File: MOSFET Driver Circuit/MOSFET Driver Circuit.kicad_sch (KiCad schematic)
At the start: 5 parts, among them Q1 NDT3055L

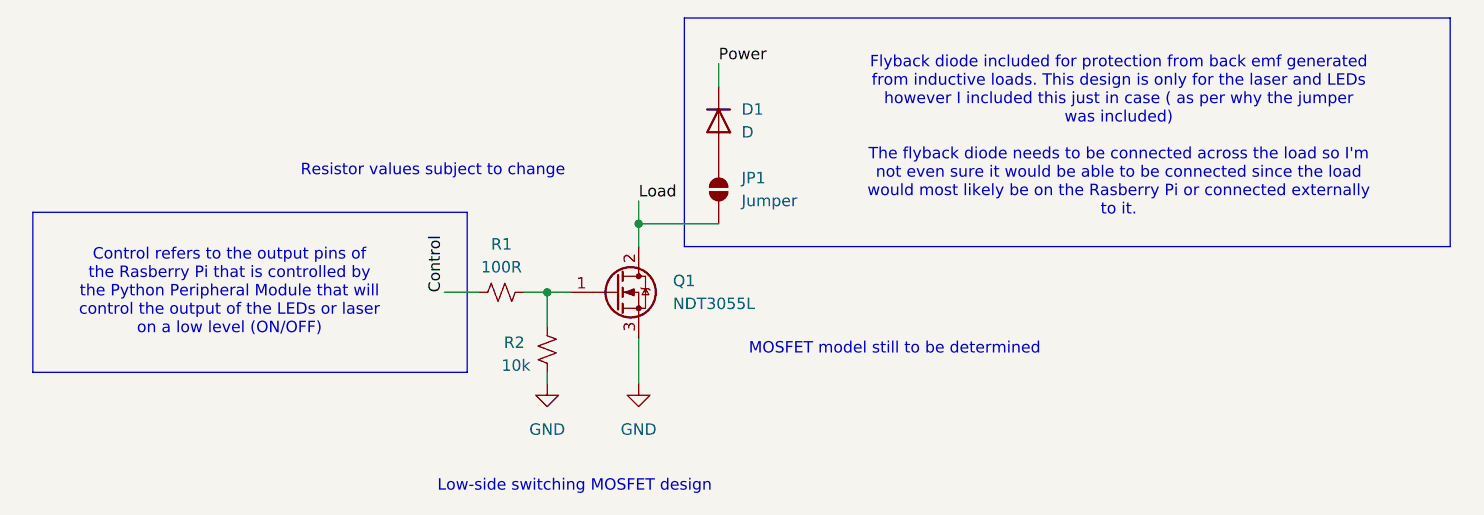
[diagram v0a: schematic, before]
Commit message: Updates
Updated the MOSFET driver circuits and created the toggle and PWM control functions for the lasers in the aqua_io.py python module

Added a relationship table for the pins on the RPi5
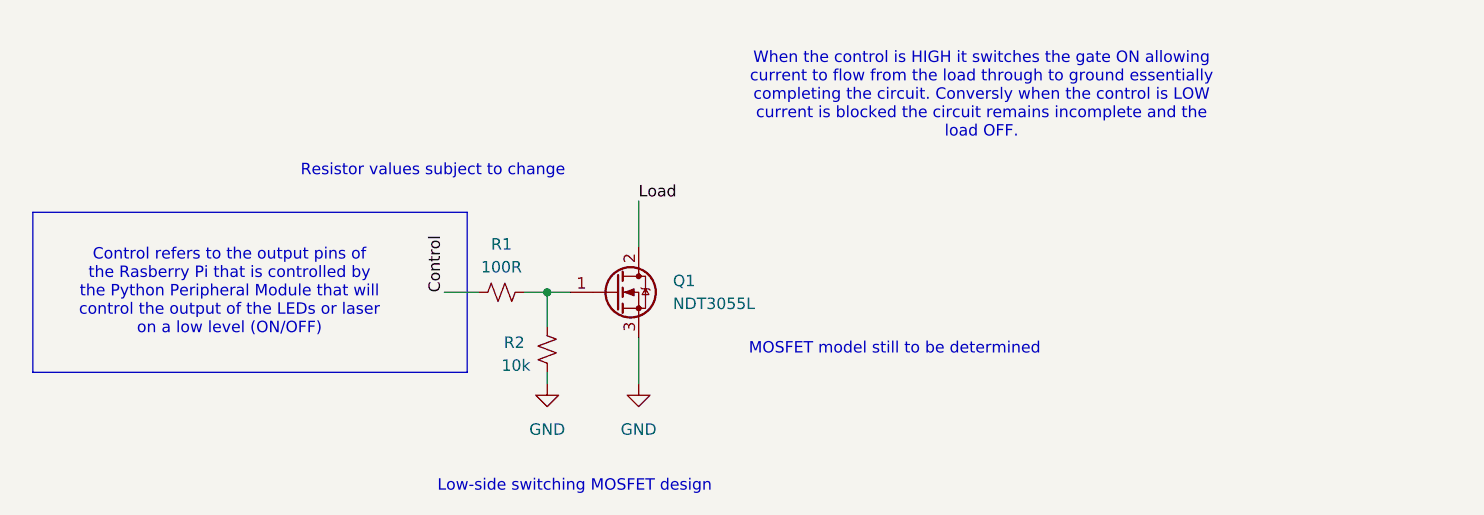
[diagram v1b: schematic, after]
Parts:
- removed D1: D, symbol Device:D
- removed JP1: Jumper, symbol Jumper:SolderJumper_2_Open
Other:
- note added: "When the control is HIGH it switches the gate ON allowing current to flow from the load through to ground essentially completing the circuit. Conversly when the control is LOW current is blocked the circuit remains incomplete and the load OFF."
- note removed: "Flyback diode included for protection from back emf generated from inductive loads. This design is only for the laser and LEDs however I included this just in case ( as per why the jumper was included) The flyback diode needs to be connected across the load so I'm not even sure it would be able to be connected since the load would most likely be on the Rasberry Pi or connected externally to it."
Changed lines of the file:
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@@
-		)
-	)
-	(rectangle
-		(start 163.83 121.92)
-		(end 248.92 147.32)
-		(stroke
-			(width 0)
-			(type default)
-		)
-		(fill
-			(type none)
 		)
 	)
@@
 		)
 	)
-	(text "Flyback diode included for protection from back emf generated \nfrom inductive loads. This design is only for the laser and LEDs\nhowever I included this just in case ( as per why the jumper\nwas included)\n\nThe flyback diode needs to be connected across the load so I'm\nnot even sure it would be able to be connected since the load\nwould most likely be on the Rasberry Pi or connected externally \nto it."
-		(exclude_from_sim no)
-		(at 212.09 135.128 0)
+	(text "When the control is HIGH it switches the gate ON allowing\ncurrent to flow from the load through to ground essentially \ncompleting the circuit. Conversly when the control is LOW \ncurrent is blocked the circuit remains incomplete and the\nload OFF."
+		(exclude_from_sim no)
+		(at 196.85 130.556 0)
 		(effects
 			(font
@@
 		(color 0 0 0 0)
 	)
-	(junction
-		(at 158.75 144.78)
-		(diameter 0)
-		(color 0 0 0 0)
-	)
 	(wire
 		(pts
@@
 	(wire
 		(pts
-			(xy 158.75 144.78) (xy 158.75 147.32)
+			(xy 158.75 142.24) (xy 158.75 147.32)
 		)
 		(stroke
@@
 	(wire
 		(pts
-			(xy 158.75 144.78) (xy 167.64 144.78)
-		)
-		(stroke
-			(width 0)
-			(type default)
-		)
-	)
-	(wire
-		(pts
 			(xy 137.16 152.4) (xy 140.97 152.4)
 		)
@@
 	(wire
 		(pts
-			(xy 158.75 142.24) (xy 158.75 144.78)
-		)
-		(stroke
-			(width 0)
-			(type default)
-		)
-	)
-	(wire
-		(pts
 			(xy 148.59 161.29) (xy 148.59 162.56)
 		)
@@
 		)
 	)
-	(wire
-		(pts
-			(xy 167.64 127) (xy 167.64 129.54)
-		)
-		(stroke
-			(width 0)
-			(type default)
+	(label "Control"
+		(at 137.16 152.4 90)
+		(effects
+			(font
+				(size 1.27 1.27)
+			)
+			(justify left bottom)
 		)
 	)
 	(label "Load"
 		(at 158.75 142.24 0)
-		(effects
-			(font
-				(size 1.27 1.27)
-			)
-			(justify left bottom)
-		)
-	)
-	(label "Control"
-		(at 137.16 152.4 90)
-		(effects
-			(font
-				(size 1.27 1.27)
-			)
-			(justify left bottom)
-		)
-	)
-	(label "Power"
-		(at 167.64 127 0)
 		(effects
 			(font
@@
 	)
 	(symbol
-		(lib_id "Device:D")
-		(at 167.64 133.35 270)
-		(unit 1)
-		(exclude_from_sim no)
-		(in_bom yes)
-		(on_board yes)
-		(dnp no)
-		(fields_autoplaced yes)
-		(property "Reference" "D1"
-			(at 170.18 132.0799 90)
-			(effects
-				(font
-					(size 1.27 1.27)
-				)
-				(justify left)
-			)
-		)
-		(property "Value" "D"
-			(at 170.18 134.6199 90)
-			(effects
-				(font
-					(size 1.27 1.27)
-				)
-				(justify left)
-			)
-		)
-		(property "Footprint" ""
-			(at 167.64 133.35 0)
-			(effects
-				(font
-					(size 1.27 1.27)
-				)
-				(hide yes)
-			)
-		)
-		(property "Datasheet" "~"
-			(at 167.64 133.35 0)
-			(effects
-				(font
-					(size 1.27 1.27)
-				)
-				(hide yes)
-			)
-		)
-		(property "Description" "Diode"
-			(at 167.64 133.35 0)
-			(effects
-				(font
-					(size 1.27 1.27)
-				)
-				(hide yes)
-			)
-		)
-		(property "Sim.Device" "D"
-			(at 167.64 133.35 0)
-			(effects
-				(font
-					(size 1.27 1.27)
-				)
-				(hide yes)
-			)
-		)
-		(property "Sim.Pins" "1=K 2=A"
-			(at 167.64 133.35 0)
-			(effects
-				(font
-					(size 1.27 1.27)
-				)
-				(hide yes)
-			)
-		)
-		(pin "2"
-		)
-		(pin "1"
-		)
-		(instances
-			(project ""
-				(path "/435687ed-7edd-4a45-a329-a0e1ed3ec891"
-					(reference "D1")
-					(unit 1)
-				)
-			)
-		)
-	)
-	(symbol
 		(lib_id "Device:R_Small_US")
 		(at 143.51 152.4 90)
@@
 					(unit 1)
 				)
-			)
-		)
-	)
-	(symbol
-		(lib_id "Jumper:SolderJumper_2_Open")
-		(at 167.64 140.97 90)
-		(unit 1)
-		(exclude_from_sim no)
-		(in_bom no)
-		(on_board yes)
-		(dnp no)
-		(fields_autoplaced yes)
-		(property "Reference" "JP1"
-			(at 170.18 139.6999 90)
-			(effects
-				(font
-					(size 1.27 1.27)
-				)
-				(justify right)
-			)
-		)
-		(property "Value" "Jumper"
-			(at 170.18 142.2399 90)
-			(effects
-				(font
-					(size 1.27 1.27)
-				)
-				(justify right)
-			)
-		)
-		(property "Footprint" ""
-			(at 167.64 140.97 0)
-			(effects
-				(font
-					(size 1.27 1.27)
-				)
-				(hide yes)
-			)
-		)
-		(property "Datasheet" "~"
-			(at 167.64 140.97 0)
-			(effects
-				(font
-					(size 1.27 1.27)
-				)
-				(hide yes)
-			)
-		)
-		(property "Description" "Solder Jumper, 2-pole, open"
-			(at 167.64 140.97 0)
-			(effects
-				(font
-					(size 1.27 1.27)
-				)
-				(hide yes)
-			)
-		)
-		(pin "2"
-		)
-		(pin "1"
-		)
-		(instances
-			(project ""
-				(path "/435687ed-7edd-4a45-a329-a0e1ed3ec891"
-					(reference "JP1")
-					(unit 1)
-				)

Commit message: Updates
Completed MOSFET driver circuit design

Removed x,y,z limit switches from aqua_io.py

Assigned more GPIO pins
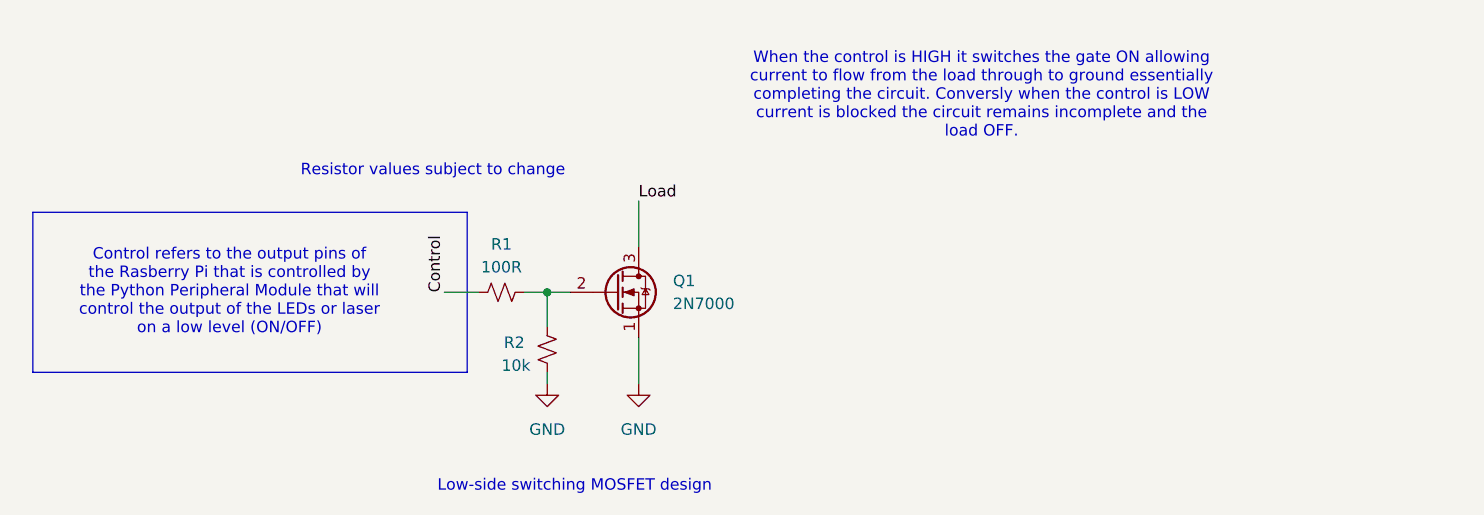
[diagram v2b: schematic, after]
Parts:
- removed Q1: NDT3055L, Package_TO_SOT_SMD:SOT-223-3_TabPin2, symbol Transistor_FET:NDT3055L
- added Q1: 2N7000, Package_TO_SOT_THT:TO-92_Inline, symbol Transistor_FET:2N7000
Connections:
- net GND: now also Q1.1 (S)
- net Load: now also Q1.3 (D)
- net at R1.2, R2.2: now also Q1.2 (G)
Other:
- note removed: "MOSFET model still to be determined"
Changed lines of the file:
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@@
-		)
-	)
-	(text "MOSFET model still to be determined"
-		(exclude_from_sim no)
-		(at 187.198 158.75 0)
-		(effects
-			(font
-				(size 1.27 1.27)
-			)
 		)
 	)
@@
 			)
 			(justify left bottom)
+		)
+	)
+	(symbol
+		(lib_id "Transistor_FET:2N7000")
+		(at 156.21 152.4 0)
+		(unit 1)
+		(exclude_from_sim no)
+		(in_bom yes)
+		(on_board yes)
+		(dnp no)
+		(fields_autoplaced yes)
+		(property "Reference" "Q1"
+			(at 162.56 151.1299 0)
+			(effects
+				(font
+					(size 1.27 1.27)
+				)
+				(justify left)
+			)
+		)
+		(property "Value" "2N7000"
+			(at 162.56 153.6699 0)
+			(effects
+				(font
+					(size 1.27 1.27)
+				)
+				(justify left)
+			)
+		)
+		(property "Footprint" "Package_TO_SOT_THT:TO-92_Inline"
+			(at 161.29 154.305 0)
+			(effects
+				(font
+					(size 1.27 1.27)
+					(italic yes)
+				)
+				(justify left)
+				(hide yes)
+			)
+		)
+		(property "Datasheet" "https://www.vishay.com/docs/70226/70226.pdf"
+			(at 161.29 156.21 0)
+			(effects
+				(font
+					(size 1.27 1.27)
+				)
+				(justify left)
+				(hide yes)
+			)
+		)
+		(property "Description" "0.2A Id, 200V Vds, N-Channel MOSFET, 2.6V Logic Level, TO-92"
+			(at 156.21 152.4 0)
+			(effects
+				(font
+					(size 1.27 1.27)
+				)
+				(hide yes)
+			)
+		)
+		(pin "3"
+		)
+		(pin "2"
+		)
+		(pin "1"
+		)
+		(instances
+			(project ""
+				(path "/435687ed-7edd-4a45-a329-a0e1ed3ec891"
+					(reference "Q1")
+					(unit 1)
+				)
+			)
 		)
 	)
@@
 					(unit 1)
 				)
-			)
-		)
-	)
-	(symbol
-		(lib_id "Transistor_FET:NDT3055L")
-		(at 156.21 152.4 0)
-		(unit 1)
-		(exclude_from_sim no)
-		(in_bom yes)
-		(on_board yes)
-		(dnp no)
-		(fields_autoplaced yes)
-		(property "Reference" "Q1"
-			(at 162.56 151.1299 0)
-			(effects
-				(font
-					(size 1.27 1.27)
-				)
-				(justify left)
-			)
-		)
-		(property "Value" "NDT3055L"
-			(at 162.56 153.6699 0)
-			(effects
-				(font
-					(size 1.27 1.27)
-				)
-				(justify left)
-			)
-		)
-		(property "Footprint" "Package_TO_SOT_SMD:SOT-223-3_TabPin2"
-			(at 161.29 154.305 0)
-			(effects
-				(font
-					(size 1.27 1.27)
-					(italic yes)
-				)
-				(justify left)
-				(hide yes)
-			)
-		)
-		(property "Datasheet" "https://www.onsemi.com/pdf/datasheet/ndt3055l-d.pdf"
-			(at 161.29 156.21 0)
-			(effects
-				(font
-					(size 1.27 1.27)
-				)
-				(justify left)
-				(hide yes)
-			)
-		)
-		(property "Description" "4A Id, 60V Vds, N-Channel Logic Level Enhancement Mode MOSFET, SOT-223"
-			(at 156.21 152.4 0)
-			(effects
-				(font
-					(size 1.27 1.27)
-				)
-				(hide yes)
-			)
-		)
-		(pin "1"
-		)
-		(pin "3"
-		)
-		(pin "2"
-		)
-		(instances
-			(project ""
-				(path "/435687ed-7edd-4a45-a329-a0e1ed3ec891"
-					(reference "Q1")
-					(unit 1)
-				)
